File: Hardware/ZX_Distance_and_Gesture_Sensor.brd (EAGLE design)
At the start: 55.9 x 15.4 mm, 46 parts, among them Q1 MMBT2222A, Q2 MOSFET-NCHANNEL2N7002PW

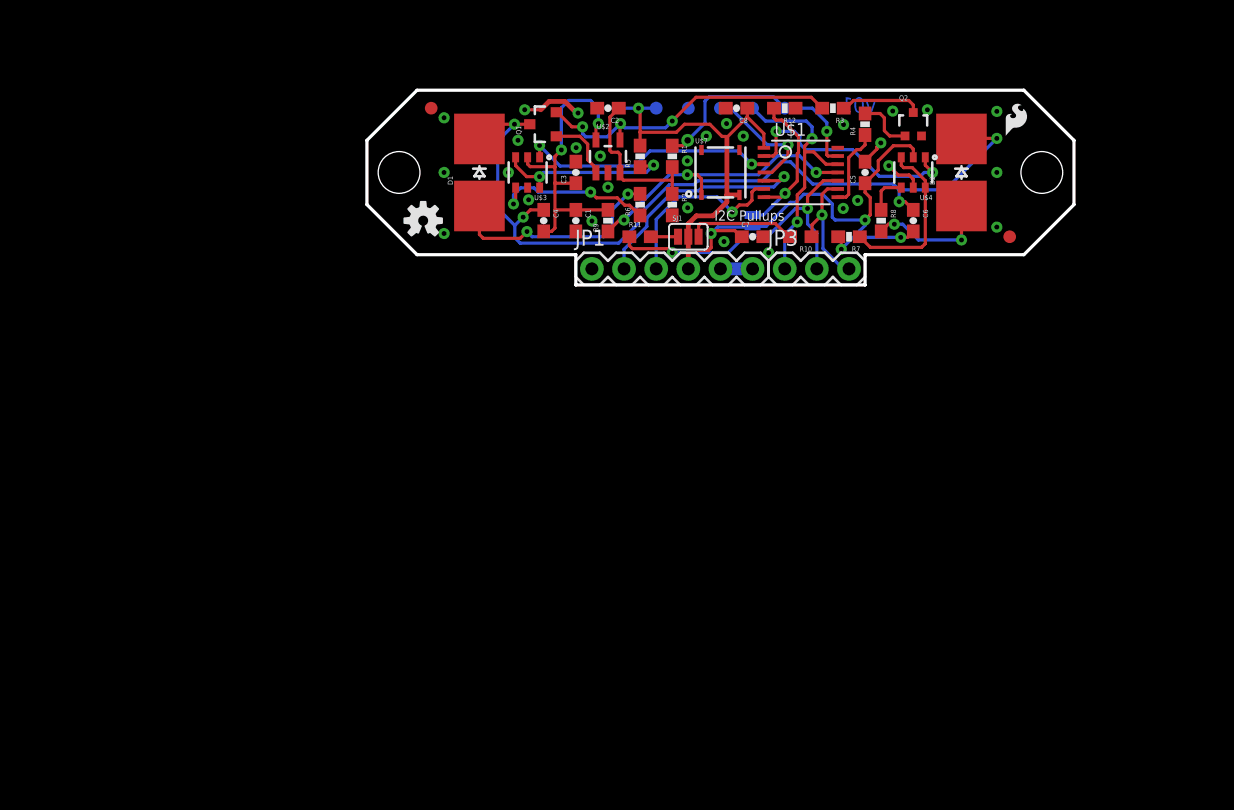
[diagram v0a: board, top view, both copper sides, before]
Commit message: Replaced SMD LEDs with PTH. Added PTH Recv'r. Ripped up traces.
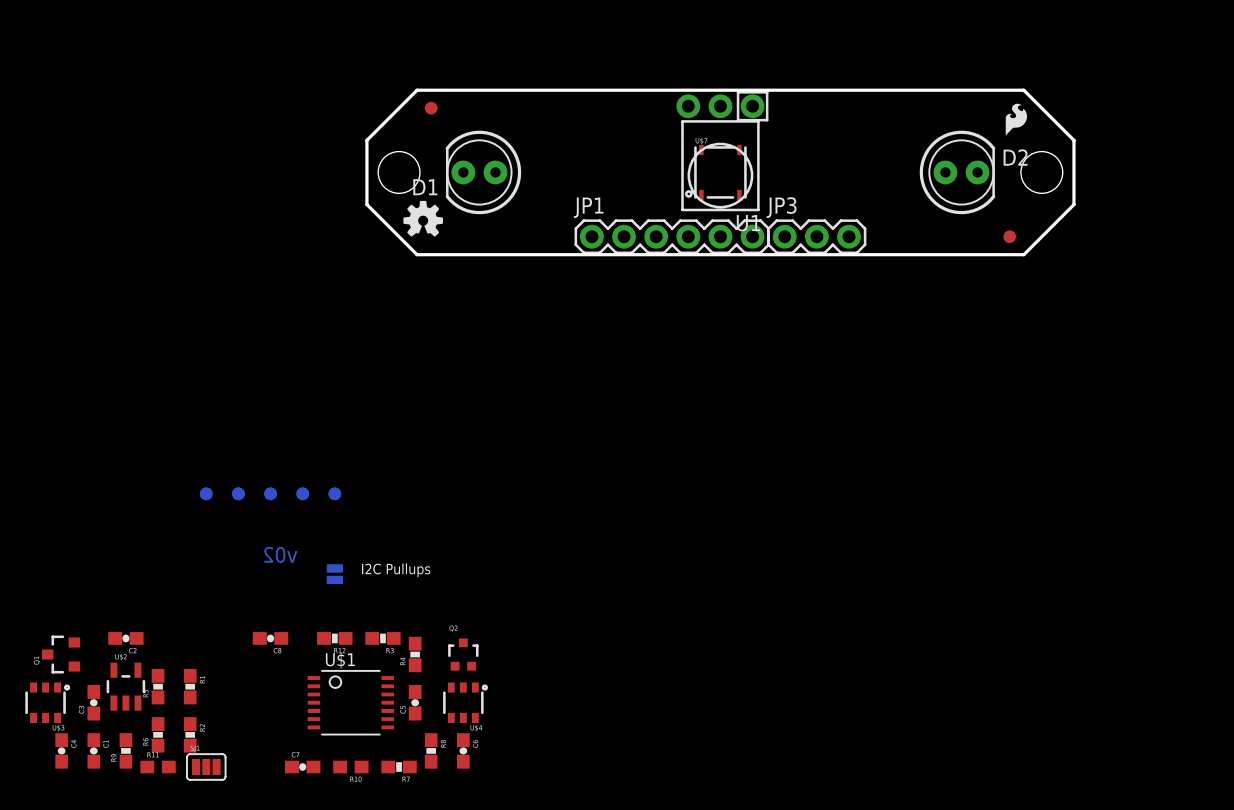
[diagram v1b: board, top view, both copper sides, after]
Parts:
- added U1: BRM-2508VERT, SparkFun-Sensors:BRM-2508_VERT
- D1, D2: value SFH4641OVERSIZE -> LED-IR-THRUTSAL6100; device SparkFun-LED:SFH4641-OVERSIZE -> SparkFun-LED:LED5MM
- moved C1 56.6 mm to (-49.5, -45.7)
- moved C2 56.6 mm to (-47.0, -36.8)
- moved C3 56.6 mm to (-49.5, -41.9)
- moved C4 56.6 mm to (-52.1, -45.7)
- moved Q1 56.6 mm to (-52.1, -38.1)
- moved R1 56.6 mm to (-41.9, -40.6)
- moved R11 56.6 mm to (-44.5, -47.0)
- moved R2 56.6 mm to (-41.9, -44.5)
- moved R5 56.6 mm to (-44.5, -40.6)
- moved R6 56.6 mm to (-44.5, -44.5)
- moved R9 56.6 mm to (-47.0, -45.7)
- moved SJ1 56.6 mm to (-40.6, -47.0)
- moved U$2 56.6 mm to (-47.0, -40.6)
- moved U$3 56.6 mm to (-53.3, -41.9)
- moved C8 55.8 mm to (-35.6, -36.8)
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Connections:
- net COMMON: now also D1.K, D2.K; no longer D1.C, D2.C
- net GND: now also U1.2
- net RECEIVER: now also U1.1
- net VCC: now also U1.3
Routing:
- net VCC: track 99.4 -> 0.03 mm, vias 7 -> 0
- net COMMON: track 66.8 -> 0.00 mm, vias 4 -> 0
- net I2C_SCL: track 25.4 -> 0.00 mm, vias 2 -> 0
- net N$2: track 25.4 -> 0.01 mm, vias 3 -> 0
- net RECEIVER: track 23.7 -> 0.00 mm, vias 3 -> 0
- net ICSPCLK/DATA_RDY: track 20.5 -> 0.00 mm, vias 2 -> 0
- net EM1: track 20.3 -> 0.00 mm, vias 2 -> 0
- net ICSPDAT/DACOUT: track 19.2 -> 0.00 mm, vias 2 -> 0
- net UART_TX: track 18.7 -> 0.00 mm, vias 1 -> 0
- net EM2: track 18.5 -> 0.00 mm, vias 2 -> 0
- net N$7: track 17.7 -> 0.00 mm, vias 2 -> 0
- net N$8: track 14.9 -> 0.00 mm, vias 2 -> 0
- net UART_RX: track 14.8 -> 0.00 mm, vias 1 -> 0
- net N$9: track 13.7 -> 0.00 mm
- net I2C_ADDR: track 13.3 -> 0.00 mm, vias 1 -> 0
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- removed copper zone on layer 1, net GND
- removed copper zone on layer 16, net GND
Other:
- board size 55.9 x 15.4 mm -> 55.9 x 13 mm
- board text added: "v02"
- board text removed: "v01"

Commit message: Grouped components in layout
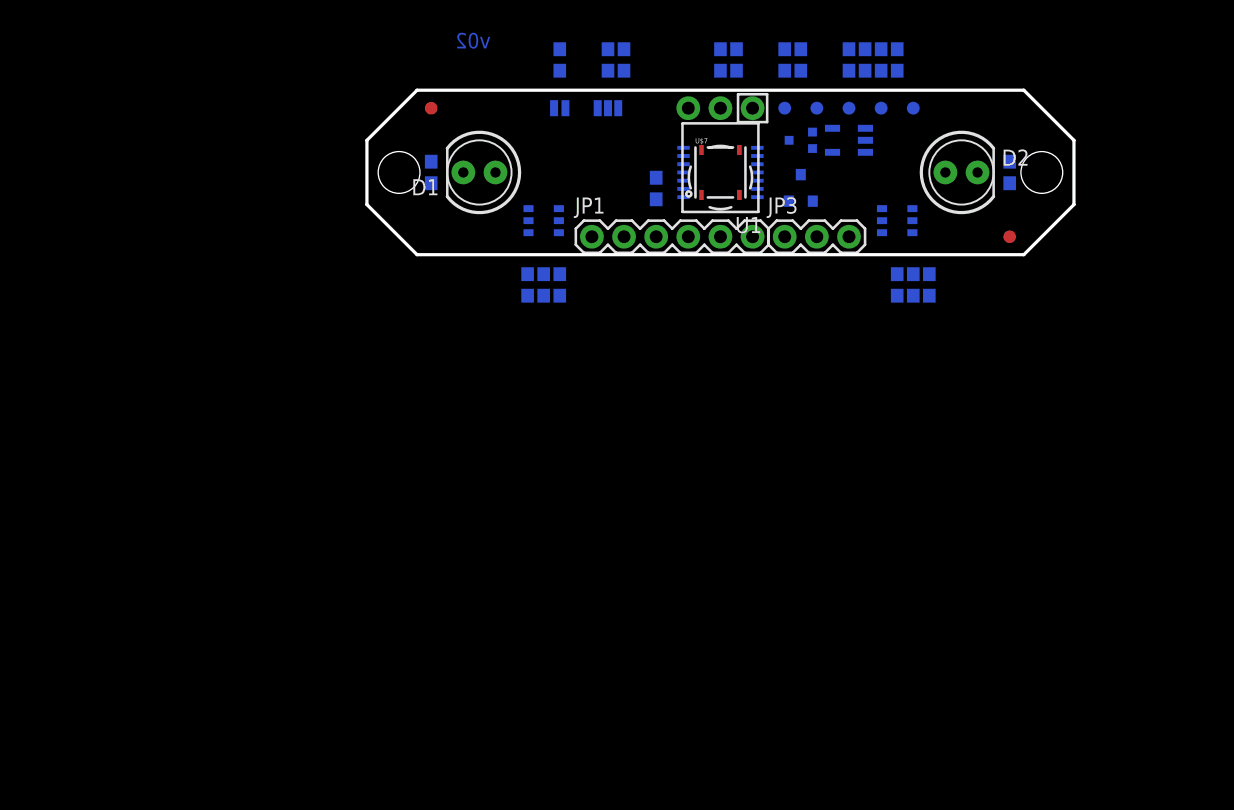
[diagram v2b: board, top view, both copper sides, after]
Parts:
- moved C1 83.8 mm to (14.0, 8.89), flipped to the bottom, turned to 90 degrees
- moved C2 75.2 mm to (12.7, 8.89), flipped to the bottom, turned to 90 degrees
- moved R2 74.5 mm to (10.2, 8.89), flipped to the bottom, turned to 90 degrees
- moved R9 72.9 mm to (1.27, 8.89), flipped to the bottom
- moved R1 72.8 mm to (11.4, 8.89), flipped to the bottom
- moved U$2 71.6 mm to (10.2, 2.54), flipped to the bottom, turned to 270 degrees
- moved Q1 69.1 mm to (6.35, -1.27), flipped to the bottom, turned to 0 degrees
- moved R11 66.2 mm to (-8.89, 8.89), flipped to the bottom, turned to 270 degrees
- moved C7 64.9 mm to (0.00, 8.89), flipped to the bottom, turned to 90 degrees
- moved C6 62.9 mm to (22.9, 0.00), flipped to the bottom
- moved TP1 61.4 mm to (12.7, 5.08)
- moved SJ1 61.0 mm to (-8.89, 5.08), flipped to the bottom, turned to 180 degrees
- moved R10 59.9 mm to (-7.62, 8.89), flipped to the bottom, turned to 270 degrees
- moved TP3 59.2 mm to (15.2, 5.08)
- moved TP2 57.1 mm to (10.2, 5.08)
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
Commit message: Initial placement of parts for v02.
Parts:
- moved LOGO2 55.3 mm to (23.5, 3.81)
- moved LOGO1 54.6 mm to (-22.2, -5.08)
- moved TP3 30.5 mm to (-15.2, 5.08)
- moved TP1 25.4 mm to (-12.7, 5.08)
- moved TP2 20.3 mm to (-10.2, 5.08)
- moved TP5 15.2 mm to (-7.62, 5.08)
- moved R6 14.2 mm to (-20.3, 3.81), turned to 270 degrees
- moved C5 13.3 mm to (17.8, 3.81), turned to 270 degrees
- moved R8 13.3 mm to (20.3, 3.81), turned to 270 degrees
- moved R9 12.6 mm to (-7.62, 0.00)
- moved R3 11.7 mm to (12.7, 0.00), turned to 270 degrees
- moved C7 10.2 mm to (-5.08, 0.00), turned to 270 degrees
- moved TP4 10.2 mm to (-5.08, 5.08)
- moved R11 9.67 mm to (-12.7, 0.00), turned to 90 degrees
- moved R10 9.25 mm to (-10.2, 0.00), turned to 90 degrees
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
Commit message: Initial layout complete for v02.
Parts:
- moved C7 2.84 mm to (-6.35, 2.54), turned to 0 degrees
- moved R9 1.27 mm to (-6.35, 0.00), turned to 180 degrees
- turned C1 to 90 degrees
- turned C8 to 0 degrees
- turned Q1 to 270 degrees
- turned SJ2 to 0 degrees
- turned U$2 to 180 degrees
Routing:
- net VCC: track 0.00 -> 96.5 mm, vias 0 -> 4
- net COMMON: track 0.00 -> 57.7 mm, vias 0 -> 2
- net ICSPDAT/DACOUT: track 0.00 -> 27.6 mm, vias 0 -> 2
- net RECEIVER: track 0.00 -> 27.5 mm, vias 0 -> 1
- net I2C_SCL: track 0.00 -> 26.7 mm, vias 0 -> 2
- net I2C_SDA: track 0.00 -> 26.7 mm, vias 0 -> 2
- net I2C_ADDR: track 0.00 -> 19.2 mm, vias 0 -> 2
- net EM2: track 0.00 -> 18.3 mm
- net MCLR: track 0.00 -> 17.8 mm, vias 0 -> 2
- net ICSPCLK/DATA_RDY: track 0.00 -> 17.6 mm, vias 0 -> 1
- net N$11: track 0.00 -> 13.7 mm, vias 0 -> 2
- net EM1: track 0.00 -> 13.0 mm, vias 0 -> 2
- net UART_TX: track 0.00 -> 13.0 mm, vias 0 -> 1
- net UART_RX: track 0.00 -> 12.8 mm, vias 0 -> 1
- net N$6: track 0.00 -> 11.7 mm, vias 0 -> 2
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- added copper zone on layer 1, net GND
- added copper zone on layer 16, net GND

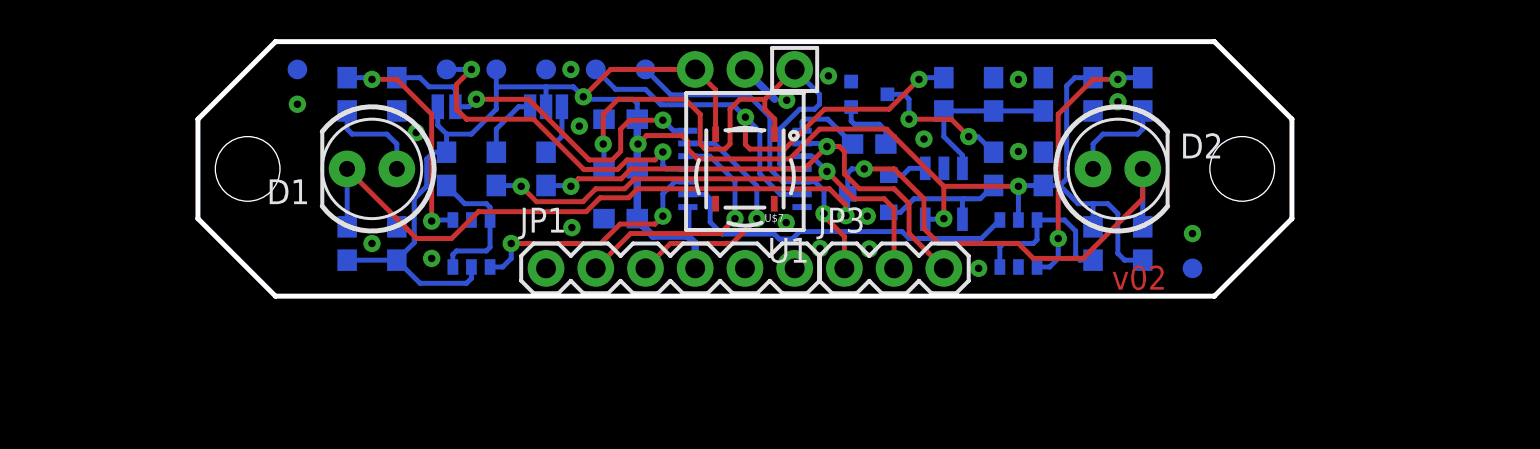
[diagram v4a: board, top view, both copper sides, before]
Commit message: Reduced board thickness
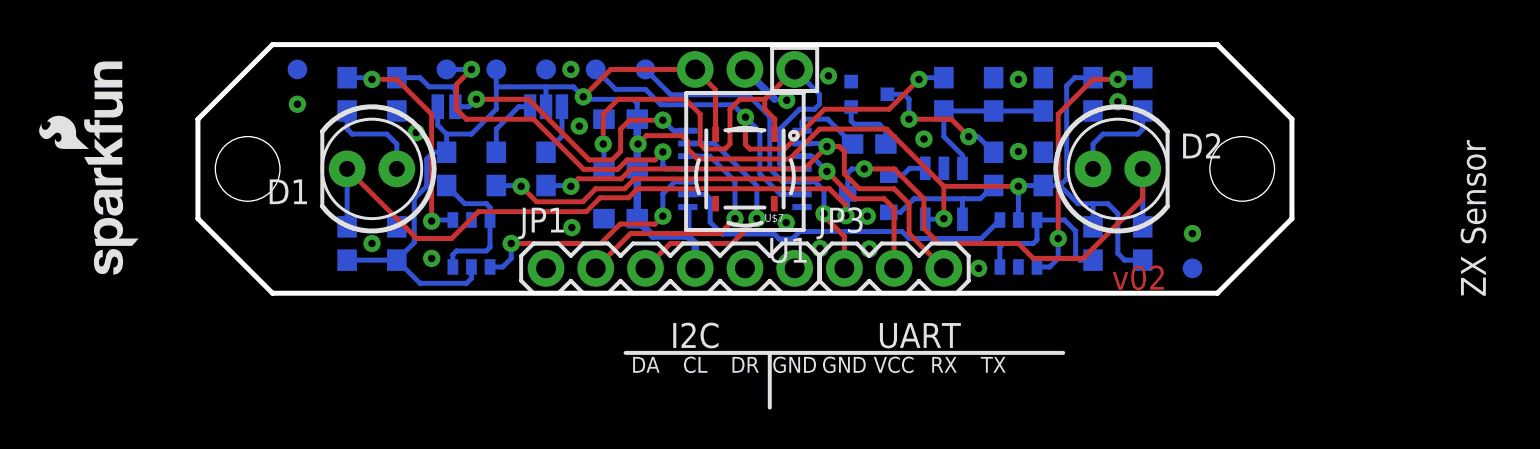
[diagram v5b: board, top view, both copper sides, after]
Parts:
- moved U$5 8.89 mm to (-30.9, -5.84), flipped to the top
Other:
- board size 55.9 x 13 mm -> 55.9 x 12.7 mm
- board text added: "I2C Addr"
- board text removed: "Op: 0x20 Cl: 0x22"
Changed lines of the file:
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@@
 <setting verticaltext="up"/>
 </settings>
-<grid distance="0.05" unitdist="inch" unit="inch" style="dots" multiple="1" display="yes" altdistance="0.025" altunitdist="inch" altunit="inch"/>
+<grid distance="0.05" unitdist="inch" unit="inch" style="dots" multiple="1" display="yes" altdistance="0.005" altunitdist="inch" altunit="inch"/>
 <layers>
 <layer number="1" name="Top" color="4" fill="1" visible="yes" active="yes"/>
@@
 <board>
 <plain>
-<wire x1="-23.979409375" y1="6.500590625" x2="23.979409375" y2="6.500590625" width="0.254" layer="20"/>
+<wire x1="-24.13" y1="6.35" x2="24.13" y2="6.35" width="0.254" layer="20"/>
 <wire x1="-14.49974375" y1="6.500590625" x2="14.50025625" y2="6.500590625" width="0.254" layer="51"/>
 <wire x1="14.50025625" y1="6.500590625" x2="14.50025625" y2="3.750590625" width="0.254" layer="51"/>
@@
 <wire x1="-18.5" y1="0" x2="18.5" y2="0" width="0.1" layer="51" style="shortdash"/>
 <wire x1="-27.94" y1="2.54" x2="-27.94" y2="-2.54" width="0.254" layer="20"/>
-<wire x1="-27.94" y1="2.54" x2="-23.979409375" y2="6.500590625" width="0.254" layer="20"/>
-<wire x1="-27.94" y1="-2.54" x2="-23.979409375" y2="-6.500590625" width="0.254" layer="20"/>
+<wire x1="-27.94" y1="2.54" x2="-24.13" y2="6.35" width="0.254" layer="20"/>
+<wire x1="-27.94" y1="-2.54" x2="-24.13" y2="-6.35" width="0.254" layer="20"/>
 <wire x1="27.94" y1="2.54" x2="27.94" y2="-2.54" width="0.254" layer="20"/>
-<wire x1="27.94" y1="-2.54" x2="23.979409375" y2="-6.500590625" width="0.254" layer="20"/>
-<wire x1="27.94" y1="2.54" x2="23.979409375" y2="6.500590625" width="0.254" layer="20"/>
-<wire x1="-23.979409375" y1="-6.499409375" x2="23.979409375" y2="-6.499409375" width="0.254" layer="20"/>
+<wire x1="27.94" y1="-2.54" x2="24.13" y2="-6.35" width="0.254" layer="20"/>
+<wire x1="27.94" y1="2.54" x2="24.13" y2="6.35" width="0.254" layer="20"/>
+<wire x1="-24.13" y1="-6.35" x2="24.13" y2="-6.35" width="0.254" layer="20"/>
 <dimension x1="-19.05" y1="0" x2="19.05" y2="0" x3="0" y3="15.24" textsize="1.778" textratio="15" layer="51" unit="inch"/>
 <dimension x1="-25.4" y1="0" x2="25.4" y2="0" x3="0" y3="19.05" textsize="1.778" textratio="15" layer="51" unit="inch"/>
 <dimension x1="-27.94" y1="2.54" x2="27.94" y2="2.54" x3="0" y3="24.13" textsize="1.778" textratio="15" layer="51" unit="inch"/>
-<dimension x1="23.979409375" y1="6.500590625" x2="23.979409375" y2="-6.500590625" x3="34.29" y3="0" textsize="1.778" textratio="15" layer="51" unit="inch"/>
-<text x="-7.62" y="-10.414" size="0.8128" layer="22" font="vector" ratio="15" rot="MR0" align="bottom-center">TX</text>
-<text x="-5.08" y="-10.414" size="0.8128" layer="22" font="vector" ratio="15" rot="MR0" align="bottom-center">RX</text>
-<text x="-2.54" y="-10.414" size="0.8128" layer="22" font="vector" ratio="15" rot="MR0" align="bottom-center">VCC</text>
-<text x="0" y="-10.414" size="0.8128" layer="22" font="vector" ratio="15" rot="MR0" align="bottom-center">GND</text>
-<text x="2.54" y="-10.414" size="0.8128" layer="22" font="vector" ratio="15" rot="MR0" align="bottom-center">GND</text>
-<text x="5.08" y="-10.414" size="0.8128" layer="22" font="vector" ratio="15" rot="MR0" align="bottom-center">DR</text>
-<text x="7.62" y="-10.414" size="0.8128" layer="22" font="vector" ratio="15" rot="MR0" align="bottom-center">CL</text>
-<text x="10.16" y="-10.414" size="0.8128" layer="22" font="vector" ratio="15" rot="MR0" align="bottom-center">DA</text>
-<wire x1="-11.176" y1="-9.398" x2="3.81" y2="-9.398" width="0.2032" layer="22"/>
-<wire x1="3.81" y1="-9.398" x2="3.81" y2="-12.192" width="0.2032" layer="22"/>
-<wire x1="3.81" y1="-9.398" x2="11.176" y2="-9.398" width="0.2032" layer="22"/>
-<text x="-3.81" y="-9.144" size="1.27" layer="22" font="vector" ratio="15" rot="MR0" align="bottom-center">UART</text>
-<text x="7.62" y="-9.144" size="1.27" layer="22" font="vector" ratio="15" rot="MR0" align="bottom-center">I2C</text>
-<text x="-14.986" y="12.954" size="0.8128" layer="22" font="vector" ratio="15" rot="MR0" align="bottom-center">Op: 0x20
-Cl: 0x22</text>
-<text x="37.846" y="-2.54" size="1.27" layer="22" font="vector" ratio="15" rot="MR90" align="bottom-center">ZX Sensor</text>
+<text x="12.7" y="-10.414" size="0.8128" layer="21" font="vector" ratio="15" align="bottom-center">TX</text>
+<text x="10.16" y="-10.414" size="0.8128" layer="21" font="vector" ratio="15" align="bottom-center">RX</text>
+<text x="7.62" y="-10.414" size="0.8128" layer="21" font="vector" ratio="15" align="bottom-center">VCC</text>
+<text x="5.08" y="-10.414" size="0.8128" layer="21" font="vector" ratio="15" align="bottom-center">GND</text>
+<text x="2.54" y="-10.414" size="0.8128" layer="21" font="vector" ratio="15" align="bottom-center">GND</text>
+<text x="0" y="-10.414" size="0.8128" layer="21" font="vector" ratio="15" align="bottom-center">DR</text>
+<text x="-2.54" y="-10.414" size="0.8128" layer="21" font="vector" ratio="15" align="bottom-center">CL</text>
+<text x="-5.08" y="-10.414" size="0.8128" layer="21" font="vector" ratio="15" align="bottom-center">DA</text>
+<wire x1="16.256" y1="-9.398" x2="1.27" y2="-9.398" width="0.2032" layer="21"/>
+<wire x1="1.27" y1="-9.398" x2="1.27" y2="-12.192" width="0.2032" layer="21"/>
+<wire x1="1.27" y1="-9.398" x2="-6.096" y2="-9.398" width="0.2032" layer="21"/>
+<text x="8.89" y="-9.144" size="1.27" layer="21" font="vector" ratio="15" align="bottom-center">UART</text>
+<text x="-2.54" y="-9.144" size="1.27" layer="21" font="vector" ratio="15" align="bottom-center">I2C</text>
+<text x="-13.462" y="0.762" size="0.8128" layer="22" font="vector" ratio="15" rot="MR270" align="bottom-center">I2C Addr</text>
+<text x="37.846" y="-2.54" size="1.27" layer="21" font="vector" ratio="15" rot="R90" align="bottom-center">ZX Sensor</text>
 <text x="20.1422" y="-5.5626" size="1.2192" layer="1" font="vector" ratio="15" rot="R180" align="center">v02</text>
-<text x="-6.604" y="12.7" size="0.8128" layer="22" font="vector" ratio="15" rot="MR0" align="bottom-center">I2C Pullups</text>
+<text x="-4.064" y="3.302" size="0.8128" layer="22" font="vector" ratio="15" rot="MR0" align="bottom-center">I2C Pullups</text>
+<dimension x1="24.13" y1="6.35" x2="24.13" y2="-6.35" x3="35.56" y3="0" textsize="1.778" textratio="15" layer="51" unit="inch"/>
 </plain>
 <attributes>
@@
 <element name="FID1" library="SparkFun-Aesthetics" package="FIDUCIAL-1X2" value="FIDUCIAL1X2" x="-22.86" y="5.08" rot="MR0"/>
 <element name="FID2" library="SparkFun-Aesthetics" package="FIDUCIAL-1X2" value="FIDUCIAL1X2" x="22.86" y="-5.08" rot="MR0"/>
-<element name="U$5" library="SparkFun-Aesthetics" package="SFE_LOGO_NAME_FLAME_.1" value="SFE_LOGO_NAME_FLAME.1_INCH" x="-39.751" y="-5.842" rot="MR90"/>
+<element name="U$5" library="SparkFun-Aesthetics" package="SFE_LOGO_NAME_FLAME_.1" value="SFE_LOGO_NAME_FLAME.1_INCH" x="-30.861" y="-5.842" rot="R90"/>
 <element name="LOGO1" library="SparkFun-Aesthetics" package="SFE_LOGO_FLAME_.1" value="SFE_LOGO_FLAME.1_INCH" x="-22.225" y="-5.08" rot="MR0"/>
 <element name="LOGO2" library="SparkFun-Aesthetics" package="OSHW-LOGO-S" value="OSHW-LOGOS" x="23.495" y="3.81" rot="MR0"/>
@@
 <contactref element="U1" pad="2"/>
 <polygon width="0.254" layer="1" isolate="0.2032">
-<vertex x="-23.9776" y="-6.5024"/>
-<vertex x="23.9776" y="-6.5024"/>
-<vertex x="27.9146" y="-2.5654"/>
+<vertex x="-24.13" y="-6.35"/>
+<vertex x="24.13" y="-6.35"/>
 <vertex x="27.94" y="-2.54"/>
 <vertex x="27.94" y="2.54"/>
-<vertex x="23.9776" y="6.5024"/>
-<vertex x="-23.9776" y="6.5024"/>
+<vertex x="24.13" y="6.35"/>
+<vertex x="-24.13" y="6.35"/>
 <vertex x="-27.94" y="2.54"/>
 <vertex x="-27.94" y="-2.54"/>
 </polygon>
 <polygon width="0.254" layer="16" isolate="0.2032">
-<vertex x="-23.9776" y="-6.5024"/>
-<vertex x="23.9776" y="-6.5024"/>
+<vertex x="-24.13" y="-6.35"/>
+<vertex x="24.13" y="-6.35"/>
 <vertex x="27.94" y="-2.54"/>
 <vertex x="27.94" y="2.54"/>
-<vertex x="23.9776" y="6.5024"/>
-<vertex x="-23.9776" y="6.5024"/>
+<vertex x="24.13" y="6.35"/>
+<vertex x="-24.13" y="6.35"/>
 <vertex x="-27.94" y="2.54"/>
 <vertex x="-27.94" y="-2.54"/>
@@
 </board>
 </drawing>
-<compatibility>
-<note version="6.3" minversion="6.2.2" severity="warning">
-Since Version 6.2.2 text objects can contain more than one line,
-which will not be processed correctly with this version.
-</note>
-</compatibility>
 </eagle>
